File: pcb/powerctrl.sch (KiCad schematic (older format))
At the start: 9 parts, among them J5 PRG, J6 LOAD, U5 PIC12(L)F1571/2, U6 MOC3020M

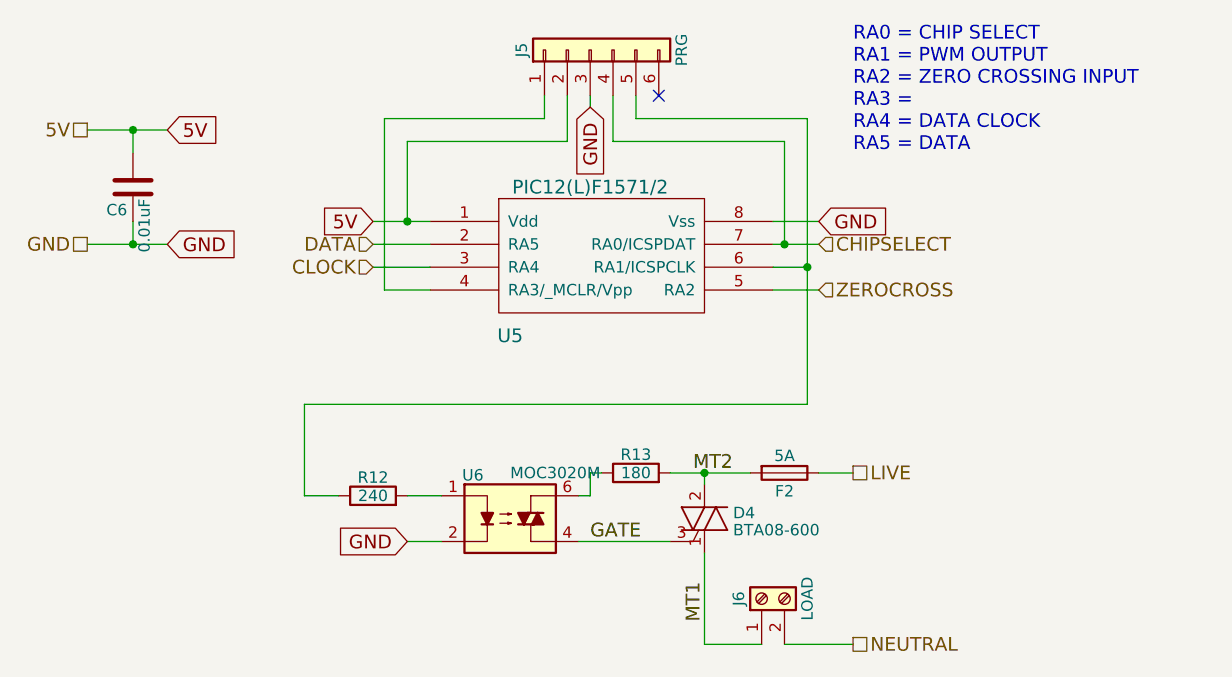
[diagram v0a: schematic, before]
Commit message: PWM1/TMR1 version
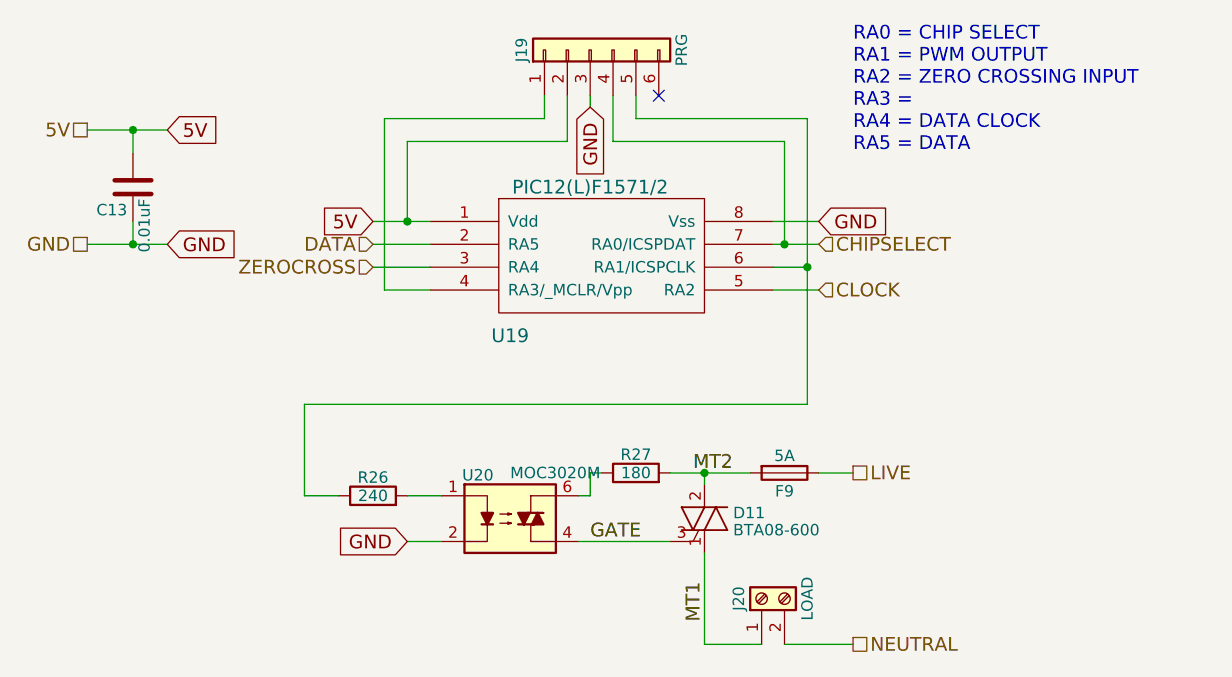
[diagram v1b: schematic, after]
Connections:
- net CLOCK: now also U5.5 (RA2); no longer U5.3 (RA4)
- net ZEROCROSS: now also U5.3 (RA4); no longer U5.5 (RA2)
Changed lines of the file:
@@
 AR Path="/5B21C6D2/5B211086" Ref="U17"  Part="1"
 AR Path="/5B21C6DE/5B211086" Ref="U19"  Part="1"
-F 0 "U5" H 4100 2500 60  0000 C CNN
+F 0 "U19" H 4100 2500 60  0000 C CNN
 F 1 "PIC12(L)F1571/2" H 4450 3150 60  0000 C CNN
 F 2 "Housings_DIP:DIP-8_W7.62mm" H 4050 2600 60  0001 C CNN
@@
 AR Path="/5B21C6D2/5B21108E" Ref="C12"  Part="1"
 AR Path="/5B21C6DE/5B21108E" Ref="C13"  Part="1"
-F 0 "C6" H 2475 2150 50  0000 L CNN
+F 0 "C13" H 2475 2150 50  0000 L CNN
 F 1 "0.01uF" V 2400 2100 50  0000 L CNN
 F 2 "Capacitors_THT:C_Disc_D3.0mm_W1.6mm_P2.50mm" H 2488 1900 50  0001 C CNN
@@
 AR Path="/5B21C6D2/5B2110AF" Ref="R24"  Part="1"
 AR Path="/5B21C6DE/5B2110AF" Ref="R26"  Part="1"
-F 0 "R12" V 3580 3400 50  0000 C CNN
+F 0 "R26" V 3580 3400 50  0000 C CNN
 F 1 "240" V 3500 3400 50  0000 C CNN
 F 2 "Resistors_THT:R_Axial_DIN0207_L6.3mm_D2.5mm_P10.16mm_Horizontal" V 3430 3400 50  0001 C CNN
@@
 AR Path="/5B21C6D2/5B2110B7" Ref="U18"  Part="1"
 AR Path="/5B21C6DE/5B2110B7" Ref="U20"  Part="1"
-F 0 "U6" H 3890 3690 50  0000 L CNN
+F 0 "U20" H 3890 3690 50  0000 L CNN
 F 1 "MOC3020M" H 4100 3700 50  0000 L CNN
 F 2 "Housings_DIP:DIP-6_W7.62mm" H 3900 3300 50  0001 L CIN
@@
 AR Path="/5B21C6D2/5B2110C1" Ref="D10"  Part="1"
 AR Path="/5B21C6DE/5B2110C1" Ref="D11"  Part="1"
-F 0 "D4" H 5075 3525 50  0000 L CNN
+F 0 "D11" H 5075 3525 50  0000 L CNN
 F 1 "BTA08-600" H 5075 3450 50  0000 L CNN
 F 2 "TO_SOT_Packages_THT:TO-220-3_Vertical" V 5025 3525 50  0001 C CNN
@@
 AR Path="/5B21C6D2/5B2110C8" Ref="R25"  Part="1"
 AR Path="/5B21C6DE/5B2110C8" Ref="R27"  Part="1"
-F 0 "R13" V 4730 3300 50  0000 C CNN
+F 0 "R27" V 4730 3300 50  0000 C CNN
 F 1 "180" V 4650 3300 50  0000 C CNN
 F 2 "Resistors_THT:R_Axial_DIN0207_L6.3mm_D2.5mm_P10.16mm_Horizontal" V 4580 3300 50  0001 C CNN
@@
 AR Path="/5B21C6D2/5B2110D5" Ref="J18"  Part="1"
 AR Path="/5B21C6DE/5B2110D5" Ref="J20"  Part="1"
-F 0 "J6" H 5200 3950 50  0000 C CNN
+F 0 "J20" H 5200 3950 50  0000 C CNN
 F 1 "LOAD" H 5200 3650 50  0000 C CNN
 F 2 "Connectors_Terminal_Blocks:TerminalBlock_bornier-2_P5.08mm" H 5200 3850 50  0001 C CNN
@@
 Text HLabel 3500 2300 0    60   Input ~ 0
 DATA
-Text HLabel 3500 2400 0    60   Input ~ 0
+Text HLabel 5450 2500 2    60   Input ~ 0
 CLOCK
 Text HLabel 5450 2300 2    60   Input ~ 0
 CHIPSELECT
-Text HLabel 5450 2500 2    60   Input ~ 0
+Text HLabel 3500 2400 0    60   Input ~ 0
 ZEROCROSS
 Text HLabel 5600 3300 2    60   UnSpc ~ 0
@@
 AR Path="/5B21C6D2/5B2B3A18" Ref="F8"  Part="1"
 AR Path="/5B21C6DE/5B2B3A18" Ref="F9"  Part="1"
-F 0 "F2" V 5380 3300 50  0000 C CNN
+F 0 "F9" V 5380 3300 50  0000 C CNN
 F 1 "5A" V 5225 3300 50  0000 C CNN
 F 2 "Fuse_Holders_and_Fuses:Fuseholder5x20_horiz_open_inline_Type-I" V 5230 3300 50  0001 C CNN
@@
 AR Path="/5B21C6D2/5B251746" Ref="J17"  Part="1"
 AR Path="/5B21C6DE/5B251746" Ref="J19"  Part="1"
-F 0 "J5" H 4450 1750 50  0000 C CNN
+F 0 "J19" H 4450 1750 50  0000 C CNN
 F 1 "PRG" H 4450 1050 50  0000 C CNN
 F 2 "Pin_Headers:Pin_Header_Straight_1x06_Pitch2.54mm" H 4450 1450 50  0001 C CNN
